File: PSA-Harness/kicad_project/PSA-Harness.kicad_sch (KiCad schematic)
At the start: 17 parts, among them J1 to_EPS_1, J10 B2B_1, J11 B2B_2, J2 to_EPS_2, J3 to_ESP_3, J4 to_car_1, J5 to_car_2, J6 to_car_3, J7 USB_C_Receptacle, J8 B2B_1, J9 B2B_2, U1 DG419LEUA, U2 DG419LEUA

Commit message: chg: schematic done
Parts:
- added D1, D2: ~, symbol PSA:BAS40SDW-AU
- added D3: SMF16A, Diode_SMD:D_SMF, symbol Diode:SMF16A
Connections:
- net +12V: now also D1.2, D1.5, D2.2, D2.5, D3.1 (A1)
- net CAN0_H: now also D1.3
- net CAN0_L: now also D1.6
- net CAN2_H: now also D2.3
- net CAN2_L: now also D2.6
- net GND: now also D1.1, D1.4, D2.1, D2.4, D3.2 (A2)
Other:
- moved on the sheet: R2, R4, U1A, U1B

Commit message: chg: components placed
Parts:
- D1, D2: value ~ -> BAS40TW-AU; footprint (none) -> Package_TO_SOT_SMD:SOT-363_SC-70-6
- D3: footprint Diode_SMD:D_SMF -> Diode_SMD:D_SOD-123
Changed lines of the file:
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@@
 		(on_board yes)
 		(dnp no)
-		(fields_autoplaced yes)
 		(property "Reference" "D1"
-			(at 205.74 132.0098 0)
+			(at 205.486 131.826 0)
 			(effects
 				(font
@@
 			)
 		)
-		(property "Value" "~"
-			(at 205.74 133.9149 0)
+		(property "Value" "BAS40TW-AU"
+			(at 210.566 134.112 0)
 			(effects
 				(font
@@
 			)
 		)
-		(property "Footprint" ""
+		(property "Footprint" "Package_TO_SOT_SMD:SOT-363_SC-70-6"
 			(at 198.12 137.16 0)
 			(effects
@@
 		(on_board yes)
 		(dnp no)
-		(fields_autoplaced yes)
 		(property "Reference" "D2"
-			(at 254 132.0098 0)
+			(at 254 131.572 0)
 			(effects
 				(font
@@
 			)
 		)
-		(property "Value" "~"
-			(at 254 133.9149 0)
+		(property "Value" "BAS40TW-AU"
+			(at 258.826 133.858 0)
 			(effects
 				(font
@@
 			)
 		)
-		(property "Footprint" ""
+		(property "Footprint" "Package_TO_SOT_SMD:SOT-363_SC-70-6"
 			(at 246.38 137.16 0)
 			(effects
@@
 			)
 		)
-		(property "Footprint" "Diode_SMD:D_SMF"
+		(property "Footprint" "Diode_SMD:D_SOD-123"
 			(at 154.94 137.16 0)
 			(effects

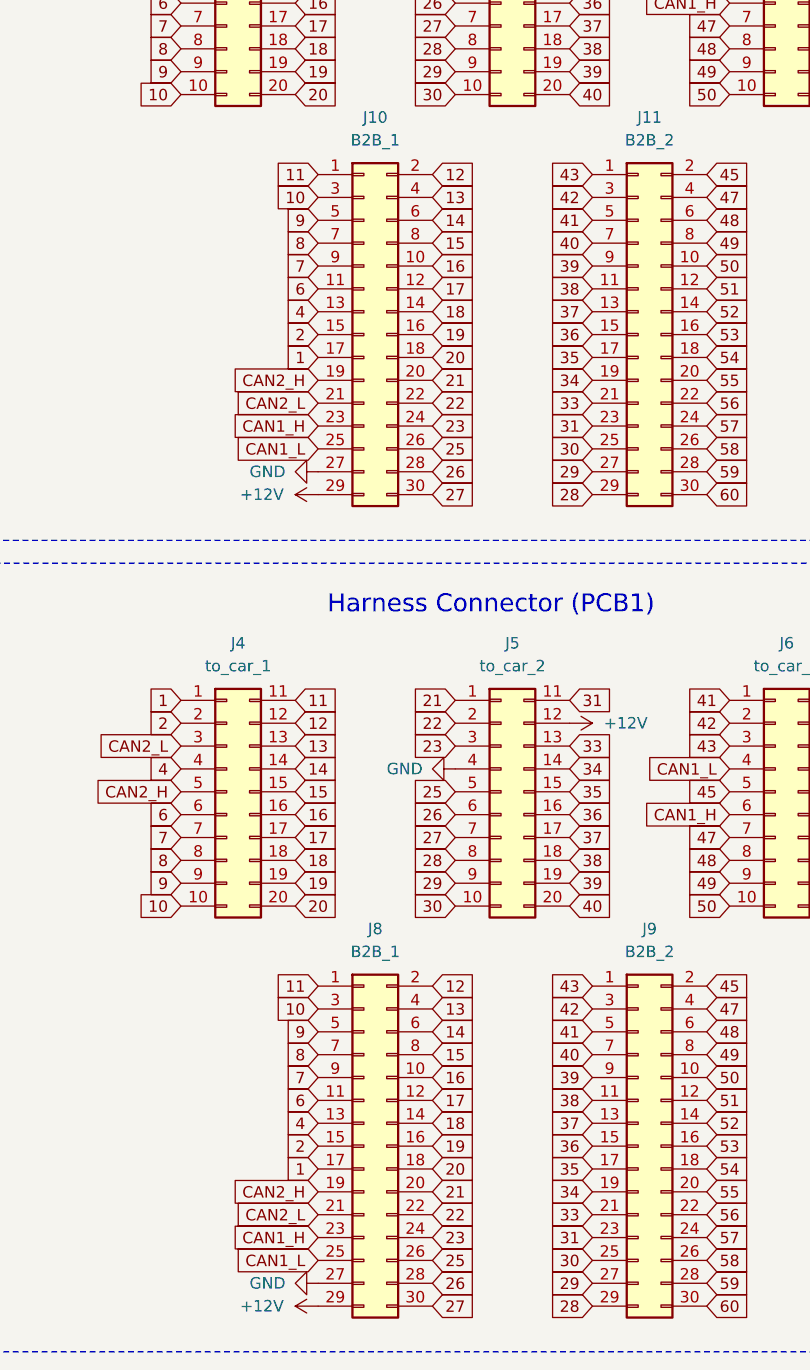
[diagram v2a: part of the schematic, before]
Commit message: chg: alternative connector DRC OK
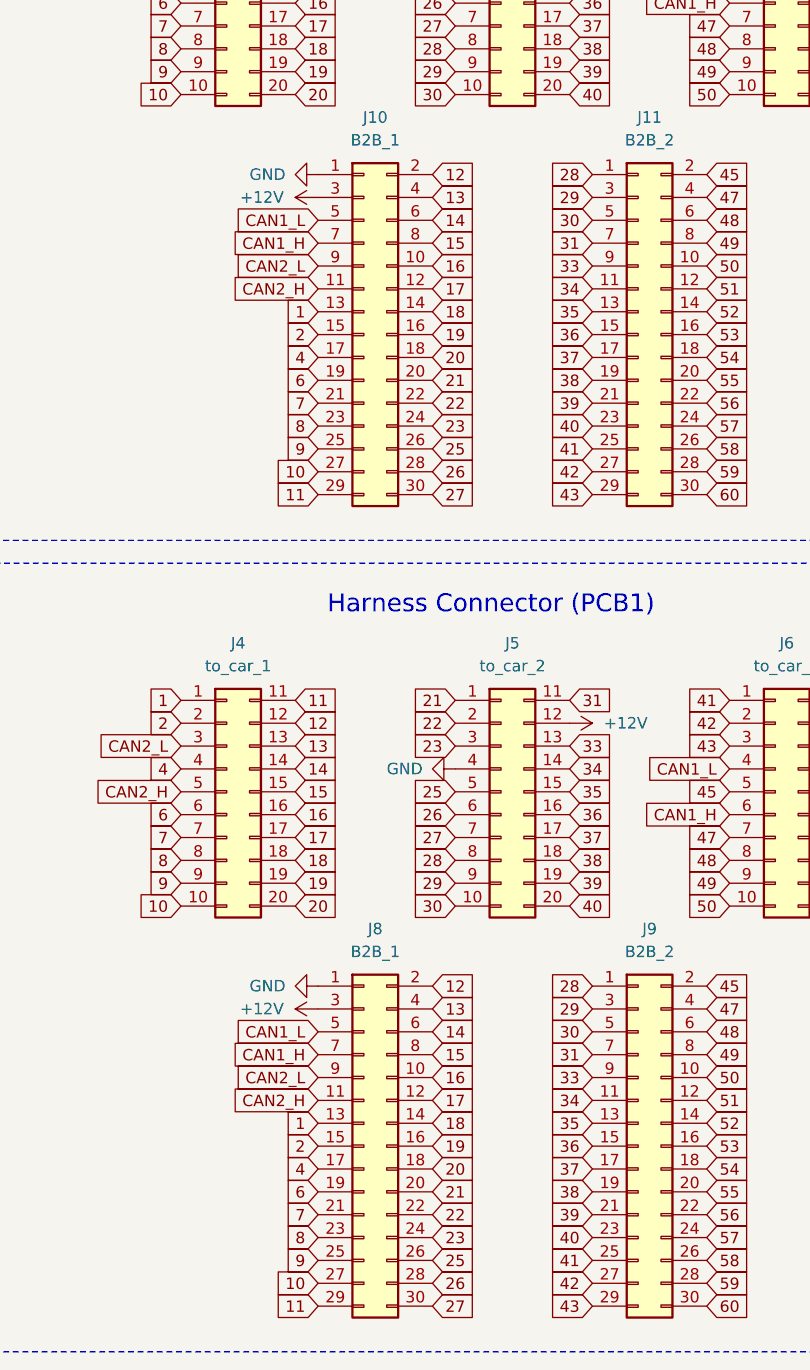
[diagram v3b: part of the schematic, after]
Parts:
- J10, J11, J8, J9: footprint Connector_PinHeader_1.27mm:PinHeader_2x15_P1.27mm_Vertical -> PSA:SAMTEC_TW-10-X-X-T-X-X
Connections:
- net +12V: now also J10.3 (Pin_3), J8.3 (Pin_3); no longer J10.29 (Pin_29), J8.29 (Pin_29)
- net 1: now also J10.13 (Pin_13), J8.13 (Pin_13); no longer J10.17 (Pin_17), J8.17 (Pin_17)
- net 10: now also J10.27 (Pin_27), J8.27 (Pin_27); no longer J10.3 (Pin_3), J8.3 (Pin_3)
- net 11: now also J10.29 (Pin_29), J8.29 (Pin_29); no longer J10.1 (Pin_1), J8.1 (Pin_1)
- net 28: now also J11.1 (Pin_1), J9.1 (Pin_1); no longer J11.29 (Pin_29), J9.29 (Pin_29)
- net 29: now also J11.3 (Pin_3), J9.3 (Pin_3); no longer J11.27 (Pin_27), J9.27 (Pin_27)
- net 30: now also J11.5 (Pin_5), J9.5 (Pin_5); no longer J11.25 (Pin_25), J9.25 (Pin_25)
- net 31: now also J11.7 (Pin_7), J9.7 (Pin_7); no longer J11.23 (Pin_23), J9.23 (Pin_23)
- net 33: now also J11.9 (Pin_9), J9.9 (Pin_9); no longer J11.21 (Pin_21), J9.21 (Pin_21)
- net 34: now also J11.11 (Pin_11), J9.11 (Pin_11); no longer J11.19 (Pin_19), J9.19 (Pin_19)
- net 35: now also J11.13 (Pin_13), J9.13 (Pin_13); no longer J11.17 (Pin_17), J9.17 (Pin_17)
- net 37: now also J11.17 (Pin_17), J9.17 (Pin_17); no longer J11.13 (Pin_13), J9.13 (Pin_13)
- net 38: now also J11.19 (Pin_19), J9.19 (Pin_19); no longer J11.11 (Pin_11), J9.11 (Pin_11)
- net 39: now also J11.21 (Pin_21), J9.21 (Pin_21); no longer J11.9 (Pin_9), J9.9 (Pin_9)
- net 4: now also J10.17 (Pin_17), J8.17 (Pin_17); no longer J10.13 (Pin_13), J8.13 (Pin_13)
- net 40: now also J11.23 (Pin_23), J9.23 (Pin_23); no longer J11.7 (Pin_7), J9.7 (Pin_7)
- net 41: now also J11.25 (Pin_25), J9.25 (Pin_25); no longer J11.5 (Pin_5), J9.5 (Pin_5)
- net 42: now also J11.27 (Pin_27), J9.27 (Pin_27); no longer J11.3 (Pin_3), J9.3 (Pin_3)
- net 43: now also J11.29 (Pin_29), J9.29 (Pin_29); no longer J11.1 (Pin_1), J9.1 (Pin_1)
- net 6: now also J10.19 (Pin_19), J8.19 (Pin_19); no longer J10.11 (Pin_11), J8.11 (Pin_11)
- net 7: now also J10.21 (Pin_21), J8.21 (Pin_21); no longer J10.9 (Pin_9), J8.9 (Pin_9)
- net 8: now also J10.23 (Pin_23), J8.23 (Pin_23); no longer J10.7 (Pin_7), J8.7 (Pin_7)
- net 9: now also J10.25 (Pin_25), J8.25 (Pin_25); no longer J10.5 (Pin_5), J8.5 (Pin_5)
- net CAN1_H: now also J10.7 (Pin_7), J8.7 (Pin_7); no longer J10.23 (Pin_23), J8.23 (Pin_23)
- net CAN1_L: now also J10.5 (Pin_5), J8.5 (Pin_5); no longer J10.25 (Pin_25), J8.25 (Pin_25)
- net CAN2_H: now also J10.11 (Pin_11), J8.11 (Pin_11); no longer J10.19 (Pin_19), J8.19 (Pin_19)
- net CAN2_L: now also J10.9 (Pin_9), J8.9 (Pin_9); no longer J10.21 (Pin_21), J8.21 (Pin_21)
- net GND: now also J10.1 (Pin_1), J8.1 (Pin_1); no longer J10.27 (Pin_27), J8.27 (Pin_27)

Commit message: chg: fix component names
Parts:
- D1, D2: value BAS40TW-AU -> BAS40SDW
- J1, J2, J3: footprint PSA:10129381-920003BLF -> PSA:Amphenol_10129381-920003BLF
- J10, J11, J8, J9: footprint PSA:SAMTEC_TW-10-X-X-T-X-X -> PSA:SAMTEC_TW-10-03-T-T-320-100
- J4, J5, J6: footprint PSA:ESW-110-44-F-D -> PSA:SAMTEC_ESW-110-44-F-D
- U1, U2: value DG419LEUA -> DG419LEDY-T1-GE4
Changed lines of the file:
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@@
 			)
 		)
-		(property "Footprint" "PSA:SAMTEC_TW-10-X-X-T-X-X"
+		(property "Footprint" "PSA:SAMTEC_TW-10-03-T-T-320-100"
 			(at 63.5 80.01 0)
 			(effects
@@
 			)
 		)
-		(property "Value" "BAS40TW-AU"
+		(property "Value" "BAS40SDW"
 			(at 210.566 134.112 0)
 			(effects
@@
 			)
 		)
-		(property "Footprint" "PSA:ESW-110-44-F-D"
+		(property "Footprint" "PSA:SAMTEC_ESW-110-44-F-D"
 			(at 109.22 130.81 0)
 			(effects
@@
 			)
 		)
-		(property "Footprint" "PSA:SAMTEC_TW-10-X-X-T-X-X"
+		(property "Footprint" "PSA:SAMTEC_TW-10-03-T-T-320-100"
 			(at 93.98 170.18 0)
 			(effects
@@
 			)
 		)
-		(property "Footprint" "PSA:10129381-920003BLF"
+		(property "Footprint" "PSA:Amphenol_10129381-920003BLF"
 			(at 78.74 40.64 0)
 			(effects
@@
 			)
 		)
-		(property "Footprint" "PSA:SAMTEC_TW-10-X-X-T-X-X"
+		(property "Footprint" "PSA:SAMTEC_TW-10-03-T-T-320-100"
 			(at 93.98 80.01 0)
 			(effects
@@
 			)
 		)
-		(property "Value" "BAS40TW-AU"
+		(property "Value" "BAS40SDW"
 			(at 258.826 133.858 0)
 			(effects
@@
 			)
 		)
-		(property "Footprint" "PSA:ESW-110-44-F-D"
+		(property "Footprint" "PSA:SAMTEC_ESW-110-44-F-D"
 			(at 78.74 130.81 0)
 			(effects
@@
 			)
 		)
-		(property "Value" "DG419LEUA"
+		(property "Value" "DG419LEDY-T1-GE4"
 			(at 187.96 62.23 0)
 			(effects
@@
 			)
 		)
-		(property "Value" "DG419LEUA"
+		(property "Value" "DG419LEDY-T1-GE4"
 			(at 187.96 20.32 0)
 			(effects
@@
 			)
 		)
-		(property "Footprint" "PSA:SAMTEC_TW-10-X-X-T-X-X"
+		(property "Footprint" "PSA:SAMTEC_TW-10-03-T-T-320-100"
 			(at 63.5 170.18 0)
 			(effects
@@
 			)
 		)
-		(property "Footprint" "PSA:ESW-110-44-F-D"
+		(property "Footprint" "PSA:SAMTEC_ESW-110-44-F-D"
 			(at 48.26 130.81 0)
 			(effects
@@
 			)
 		)
-		(property "Value" "DG419LEUA"
+		(property "Value" "DG419LEDY-T1-GE4"
 			(at 187.96 82.55 90)
 			(effects
@@
 			)
 		)
-		(property "Footprint" "PSA:10129381-920003BLF"
+		(property "Footprint" "PSA:Amphenol_10129381-920003BLF"
 			(at 48.26 40.64 0)
 			(effects
@@
 			)
 		)
-		(property "Footprint" "PSA:10129381-920003BLF"
+		(property "Footprint" "PSA:Amphenol_10129381-920003BLF"
 			(at 109.22 40.64 0)
 			(effects
@@
 			)
 		)
-		(property "Value" "DG419LEUA"
+		(property "Value" "DG419LEDY-T1-GE4"
 			(at 187.96 40.64 90)
 			(effects

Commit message: cleanup doc files
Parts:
- U1, U2: value DG419LEDY-T1-GE4 -> DG419LEDQ-T1-GE3
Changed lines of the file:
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@@
 			)
 		)
-		(property "Value" "DG419LEDY-T1-GE4"
+		(property "Value" "DG419LEDQ-T1-GE3"
 			(at 187.96 62.23 0)
 			(effects
@@
 			)
 		)
-		(property "Value" "DG419LEDY-T1-GE4"
+		(property "Value" "DG419LEDQ-T1-GE3"
 			(at 187.96 20.32 0)
 			(effects
@@
 			)
 		)
-		(property "Value" "DG419LEDY-T1-GE4"
+		(property "Value" "DG419LEDQ-T1-GE3"
 			(at 187.96 82.55 90)
 			(effects
@@
 			)
 		)
-		(property "Value" "DG419LEDY-T1-GE4"
+		(property "Value" "DG419LEDQ-T1-GE3"
 			(at 187.96 40.64 90)
 			(effects

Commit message: change footprint of analog switch from msop to soic
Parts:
- U1, U2: value DG419LEDQ-T1-GE3 -> DG419LEDQ-T1-GE4; footprint Package_SO:MSOP-8_3x3mm_P0.65mm -> Package_SO:SOIC-8_3.9x4.9mm_P1.27mm
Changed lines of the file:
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@@
 			)
 		)
-		(property "Value" "DG419LEDQ-T1-GE3"
+		(property "Value" "DG419LEDQ-T1-GE4"
 			(at 187.96 62.23 0)
 			(effects
@@
 			)
 		)
-		(property "Footprint" "Package_SO:MSOP-8_3x3mm_P0.65mm"
+		(property "Footprint" "Package_SO:SOIC-8_3.9x4.9mm_P1.27mm"
 			(at 191.135 82.55 0)
 			(effects
@@
 			)
 		)
-		(property "Value" "DG419LEDQ-T1-GE3"
+		(property "Value" "DG419LEDQ-T1-GE4"
 			(at 187.96 20.32 0)
 			(effects
@@
 			)
 		)
-		(property "Footprint" "Package_SO:MSOP-8_3x3mm_P0.65mm"
+		(property "Footprint" "Package_SO:SOIC-8_3.9x4.9mm_P1.27mm"
 			(at 191.135 40.64 0)
 			(effects
@@
 			)
 		)
-		(property "Value" "DG419LEDQ-T1-GE3"
+		(property "Value" "DG419LEDQ-T1-GE4"
 			(at 187.96 82.55 90)
 			(effects
@@
 			)
 		)
-		(property "Footprint" "Package_SO:MSOP-8_3x3mm_P0.65mm"
+		(property "Footprint" "Package_SO:SOIC-8_3.9x4.9mm_P1.27mm"
 			(at 201.93 88.265 0)
 			(effects
@@
 			)
 		)
-		(property "Value" "DG419LEDQ-T1-GE3"
+		(property "Value" "DG419LEDQ-T1-GE4"
 			(at 187.96 40.64 90)
 			(effects
@@
 			)
 		)
-		(property "Footprint" "Package_SO:MSOP-8_3x3mm_P0.65mm"
+		(property "Footprint" "Package_SO:SOIC-8_3.9x4.9mm_P1.27mm"
 			(at 201.93 46.355 0)
 			(effects
